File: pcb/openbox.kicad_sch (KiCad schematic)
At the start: 23 parts, among them J1 Conn_01x04_Male, J10 Conn_01x04_Male, J11 Conn_01x05_Male, J12 Conn_01x04_Male, J13 Conn_02x10_Odd_Even, J2 Conn_01x02_Male, J3 ST01x05, J4 ST01x05, J5 ST01x05, J6 ST01x05, J7 Conn_01x04_Male, J8 Conn_01x04_Male, J9 Conn_01x04_Male, U1 Pico, U2 SN74LV1T34DBV

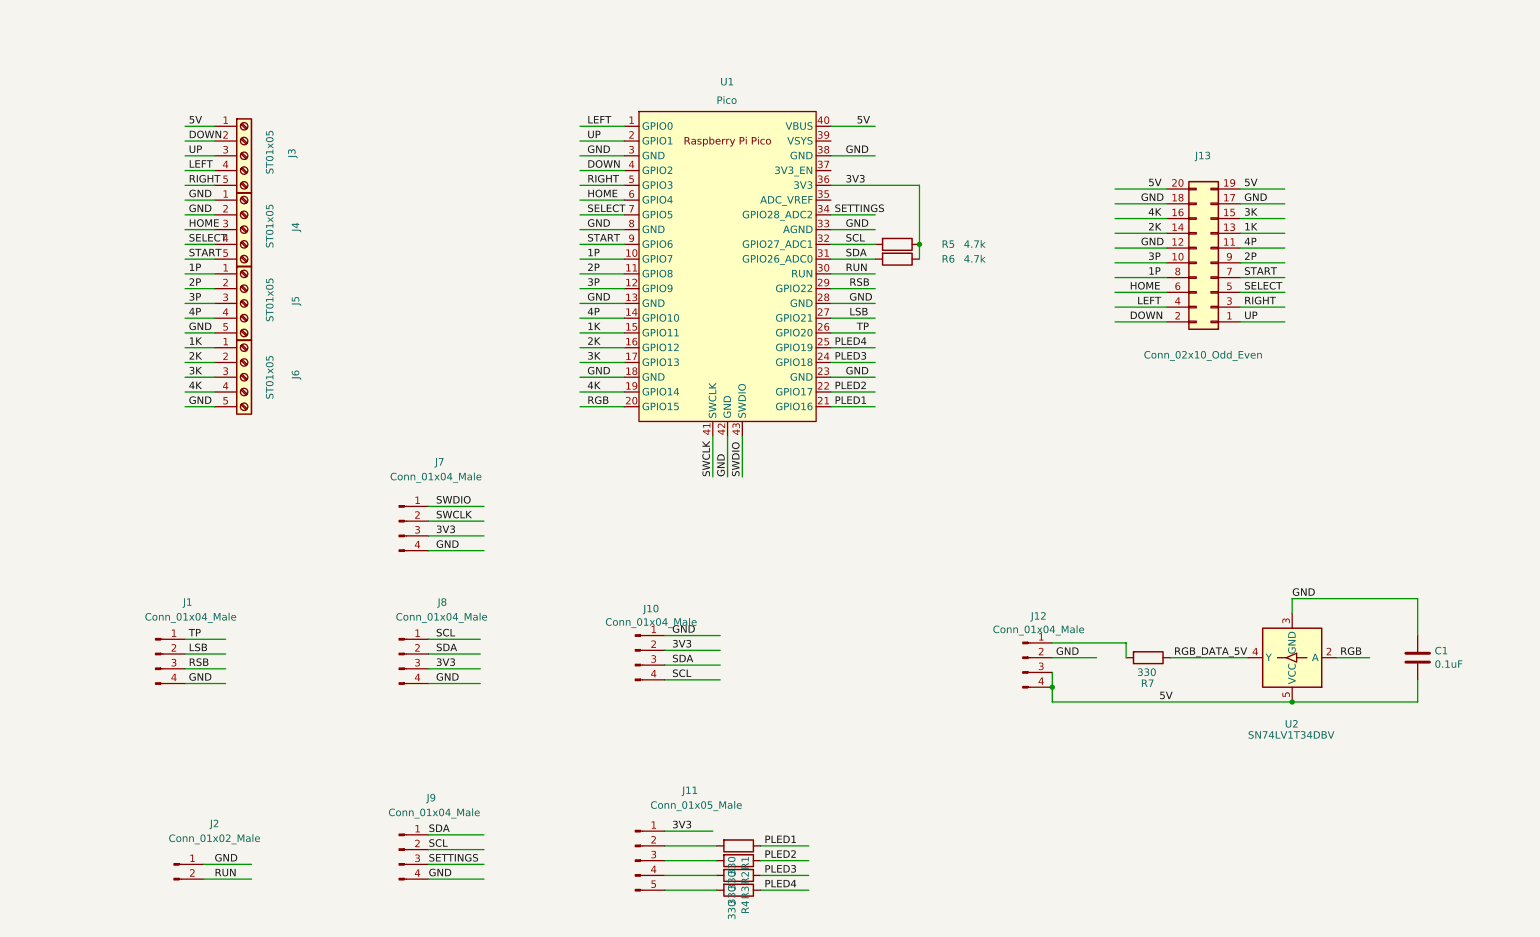
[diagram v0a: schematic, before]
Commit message: Pi placed, just have to place buttons
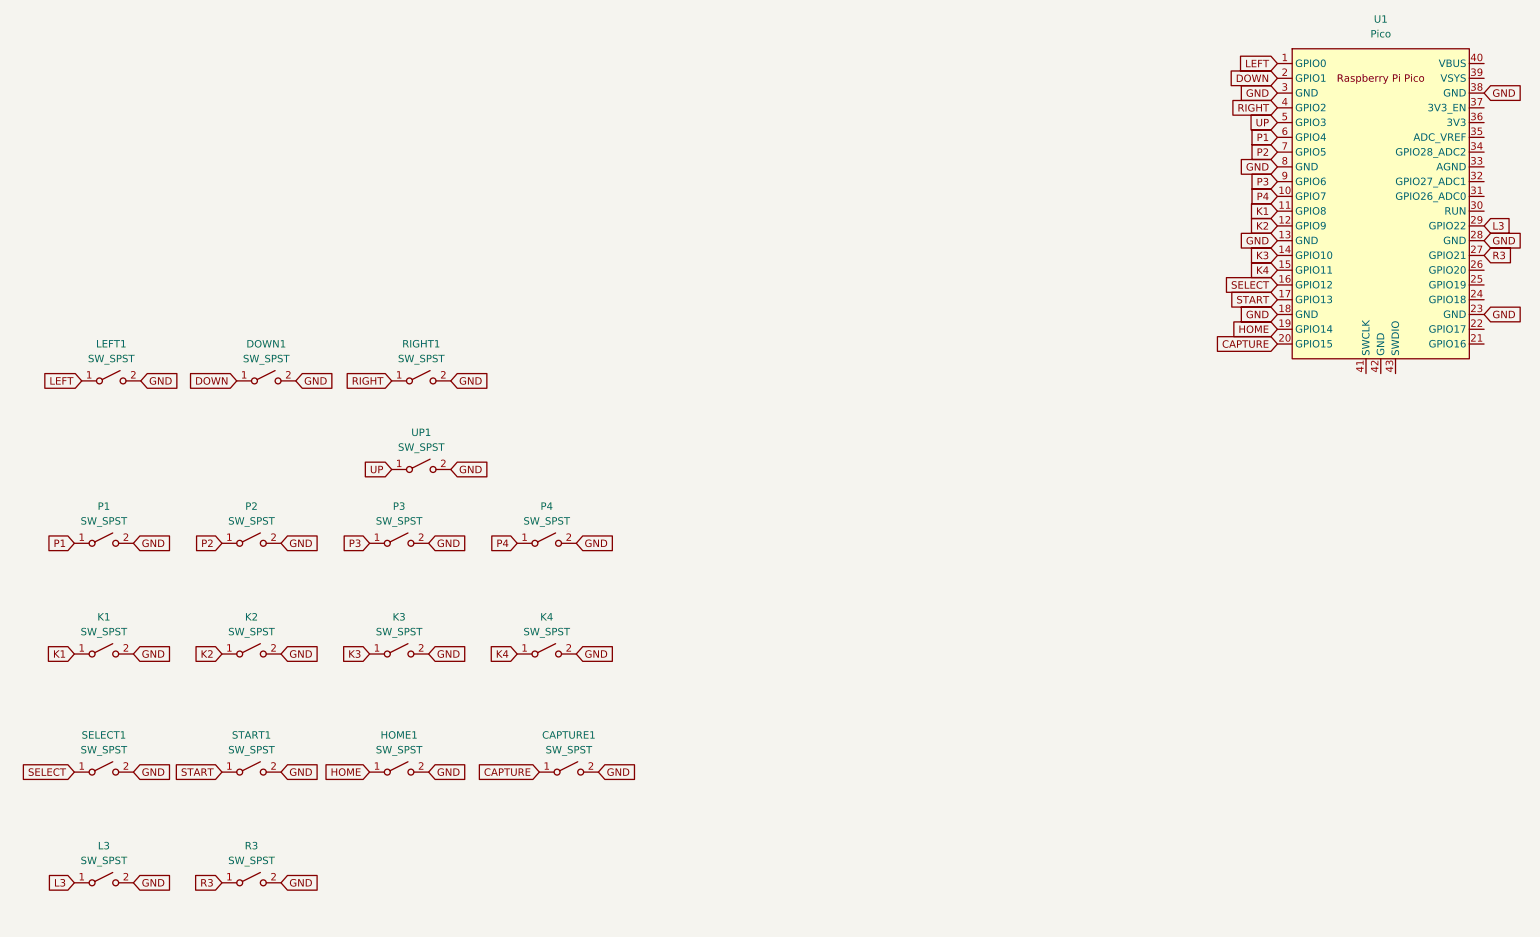
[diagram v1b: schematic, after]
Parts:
- removed C1: 0.1uF, Capacitor_SMD:C_0805_2012Metric, symbol Device:C
- removed J1, J10, J12, J9: Conn_01x04_Male, Connector_JST:JST_PH_B4B-PH-K_1x04_P2.00mm_Vertical, symbol Connector:Conn_01x04_Male
- removed J11: Conn_01x05_Male, Connector_JST:JST_PH_B5B-PH-K_1x05_P2.00mm_Vertical, symbol Connector:Conn_01x05_Male
- removed J13: Conn_02x10_Odd_Even, Connector_PinHeader_2.54mm:PinHeader_2x10_P2.54mm_Vertical, symbol Connector_Generic:Conn_02x10_Odd_Even
- removed J2: Conn_01x02_Male, Connector_PinHeader_2.54mm:PinHeader_1x02_P2.54mm_Vertical, symbol Connector:Conn_01x02_Male
- removed J3, J4, J5, J6: ST01x05, TerminalBlock_MetzConnect:TerminalBlock_MetzConnect_Type059_RT06305HBWC_1x05_P3.50mm_Horizontal, symbol Connector:Screw_Terminal_01x05
- removed J7, J8: Conn_01x04_Male, FeralAI:BOOM_SH_C145961_1x04_P1.00mm_Vertical, symbol Connector:Conn_01x04_Male
- removed R1, R2, R3, R4, R7: 330, Resistor_SMD:R_0805_2012Metric, symbol Device:R
- removed R5, R6: 4.7k, Resistor_SMD:R_0805_2012Metric, symbol Device:R
- removed U2: SN74LV1T34DBV, Package_TO_SOT_SMD:SOT-23-5, symbol Logic_LevelTranslator:SN74LV1T34DBV
- added CAPTURE1, DOWN1, HOME1, K1, K2, K3, K4, L3, LEFT1, P1, P2, P3, P4, R3, RIGHT1, SELECT1, START1, UP1: SW_SPST, keyswitches.pretty:Kailh_socket_PG1350, symbol Switch:SW_SPST
- U1: footprint MCU_RaspberryPi_and_Boards:RPi_Pico_SMD_TH_Clean -> MCU_RaspberryPi_and_Boards:RPi_Pico_SMD_TH
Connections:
- net 2K is gone; now on net SELECT: U1.16 (GPIO12)
- net 3K is gone; now on net START: U1.17 (GPIO13)
- net 4K is gone; now on net HOME: U1.19 (GPIO14)
- net DOWN: now also U1.2 (GPIO1), DOWN1.1 (A); no longer U1.4 (GPIO2)
- net GND: now also CAPTURE1.2 (B), DOWN1.2 (B), HOME1.2 (B), K1.2 (B), K2.2 (B), K3.2 (B), K4.2 (B), L3.2 (B), LEFT1.2 (B), P1.2 (B), P2.2 (B), P3.2 (B), P4.2 (B), R3.2 (B), RIGHT1.2 (B), SELECT1.2 (B), START1.2 (B), UP1.2 (B); no longer U1.33 (AGND), U1.42 (GND)
- net HOME: now also HOME1.1 (A); no longer U1.6 (GPIO4)
- net LEFT: now also LEFT1.1 (A)
- net RIGHT: now also U1.4 (GPIO2), RIGHT1.1 (A); no longer U1.5 (GPIO3)
- net SELECT: now also SELECT1.1 (A); no longer U1.7 (GPIO5)
- net START: now also START1.1 (A); no longer U1.9 (GPIO6)
- net UP: now also U1.5 (GPIO3), UP1.1 (A); no longer U1.2 (GPIO1)
- net 1K renamed K4
- net K4: now also K4.1 (A)
- net 1P renamed P4
- net P4: now also P4.1 (A)
- net 2P renamed K1
- net K1: now also K1.1 (A)
- net 3P renamed K2
- net K2: now also K2.1 (A)
- net 3V3: no longer names the net of U1.36 (3V3)
- net 4P renamed K3
- net K3: now also K3.1 (A)
- net 5V: no longer names the net of U1.40 (VBUS)
- net LSB renamed R3
- net R3: now also R3.1 (A)
- net PLED1: no longer names the net of U1.21 (GPIO16)
- net PLED2: no longer names the net of U1.22 (GPIO17)
- net PLED3: no longer names the net of U1.24 (GPIO18)
- net PLED4: no longer names the net of U1.25 (GPIO19)
- net RGB renamed CAPTURE
- net CAPTURE: now also CAPTURE1.1 (A)
- net RSB renamed L3
- net L3: now also L3.1 (A)
- net RUN: no longer names the net of U1.30 (RUN)
- net SCL: no longer names the net of U1.32 (GPIO27_ADC1)
- net SDA: no longer names the net of U1.31 (GPIO26_ADC0)
- net SETTINGS: no longer names the net of U1.34 (GPIO28_ADC2)
- net SWCLK: no longer names the net of U1.41 (SWCLK)
- net SWDIO: no longer names the net of U1.43 (SWDIO)
- net TP: no longer names the net of U1.26 (GPIO20)
- new net P1: P1.1 (A), U1.6 (GPIO4)
- new net P2: P2.1 (A), U1.7 (GPIO5)
- new net P3: P3.1 (A), U1.9 (GPIO6)

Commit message: Change extra buttons to 6x6mm push buttons
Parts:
- CAPTURE1, HOME1, L3, R3, SELECT1, START1: footprint keyswitches.pretty:Kailh_socket_PG1350 -> Button_Switch_THT:SW_PUSH_6mm
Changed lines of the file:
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@@
     (property "Reference" "START1" (id 0) (at 54.61 153.67 0))
     (property "Value" "SW_SPST" (id 1) (at 54.61 156.21 0))
-    (property "Footprint" "keyswitches.pretty:Kailh_socket_PG1350" (id 2) (at 54.61 160.02 0)
+    (property "Footprint" "Button_Switch_THT:SW_PUSH_6mm" (id 2) (at 54.61 160.02 0)
       (effects (font (size 1.27 1.27)) hide)
     )
@@
     (property "Reference" "HOME1" (id 0) (at 80.01 153.67 0))
     (property "Value" "SW_SPST" (id 1) (at 80.01 156.21 0))
-    (property "Footprint" "keyswitches.pretty:Kailh_socket_PG1350" (id 2) (at 80.01 160.02 0)
+    (property "Footprint" "Button_Switch_THT:SW_PUSH_6mm" (id 2) (at 80.01 160.02 0)
       (effects (font (size 1.27 1.27)) hide)
     )
@@
     (property "Reference" "CAPTURE1" (id 0) (at 109.22 153.67 0))
     (property "Value" "SW_SPST" (id 1) (at 109.22 156.21 0))
-    (property "Footprint" "keyswitches.pretty:Kailh_socket_PG1350" (id 2) (at 109.22 160.02 0)
+    (property "Footprint" "Button_Switch_THT:SW_PUSH_6mm" (id 2) (at 109.22 160.02 0)
       (effects (font (size 1.27 1.27)) hide)
     )
@@
     (property "Reference" "SELECT1" (id 0) (at 29.21 153.67 0))
     (property "Value" "SW_SPST" (id 1) (at 29.21 156.21 0))
-    (property "Footprint" "keyswitches.pretty:Kailh_socket_PG1350" (id 2) (at 29.21 160.02 0)
+    (property "Footprint" "Button_Switch_THT:SW_PUSH_6mm" (id 2) (at 29.21 160.02 0)
       (effects (font (size 1.27 1.27)) hide)
     )
@@
     (property "Reference" "L3" (id 0) (at 29.21 172.72 0))
     (property "Value" "SW_SPST" (id 1) (at 29.21 175.26 0))
-    (property "Footprint" "keyswitches.pretty:Kailh_socket_PG1350" (id 2) (at 29.21 179.07 0)
+    (property "Footprint" "Button_Switch_THT:SW_PUSH_6mm" (id 2) (at 29.21 179.07 0)
       (effects (font (size 1.27 1.27)) hide)
     )
@@
     (property "Reference" "R3" (id 0) (at 54.61 172.72 0))
     (property "Value" "SW_SPST" (id 1) (at 54.61 175.26 0))
-    (property "Footprint" "keyswitches.pretty:Kailh_socket_PG1350" (id 2) (at 54.61 179.07 0)
+    (property "Footprint" "Button_Switch_THT:SW_PUSH_6mm" (id 2) (at 54.61 179.07 0)
       (effects (font (size 1.27 1.27)) hide)
     )
@@
   (symbol_instances
     (path "/542d0816-e5c3-4b0c-9fe6-a8befec1abb6"
-      (reference "CAPTURE1") (unit 1) (value "SW_SPST") (footprint "keyswitches.pretty:Kailh_socket_PG1350")
+      (reference "CAPTURE1") (unit 1) (value "SW_SPST") (footprint "Button_Switch_THT:SW_PUSH_6mm")
     )
     (path "/95df881d-f66e-40ba-bb34-b870660a1b3b"
@@
     )
     (path "/3f368872-dbe5-48d5-b1bb-c08d1f5e0dd2"
-      (reference "HOME1") (unit 1) (value "SW_SPST") (footprint "keyswitches.pretty:Kailh_socket_PG1350")
+      (reference "HOME1") (unit 1) (value "SW_SPST") (footprint "Button_Switch_THT:SW_PUSH_6mm")
     )
     (path "/736c80fe-01fb-4783-a2be-9e16fccbf781"
@@
     )
     (path "/f1b2b416-be79-4848-8079-c1cc5017a182"
-      (reference "L3") (unit 1) (value "SW_SPST") (footprint "keyswitches.pretty:Kailh_socket_PG1350")
+      (reference "L3") (unit 1) (value "SW_SPST") (footprint "Button_Switch_THT:SW_PUSH_6mm")
     )
     (path "/8c2504d2-1b97-4d06-946f-3cb4a9d80e8a"
@@
     )
     (path "/f8df1ab9-c821-41ea-baed-1980e5d9f217"
-      (reference "R3") (unit 1) (value "SW_SPST") (footprint "keyswitches.pretty:Kailh_socket_PG1350")
+      (reference "R3") (unit 1) (value "SW_SPST") (footprint "Button_Switch_THT:SW_PUSH_6mm")
     )
     (path "/6087dd73-6174-4d62-9d84-8dd5c28de338"
@@
     )
     (path "/c40dde26-fffd-4a43-a9b1-f178e1e494f3"
-      (reference "SELECT1") (unit 1) (value "SW_SPST") (footprint "keyswitches.pretty:Kailh_socket_PG1350")
+      (reference "SELECT1") (unit 1) (value "SW_SPST") (footprint "Button_Switch_THT:SW_PUSH_6mm")
     )
     (path "/3c4412bc-b78d-459f-9f44-573a3673fb1a"
-      (reference "START1") (unit 1) (value "SW_SPST") (footprint "keyswitches.pretty:Kailh_socket_PG1350")
+      (reference "START1") (unit 1) (value "SW_SPST") (footprint "Button_Switch_THT:SW_PUSH_6mm")
     )
     (path "/b7eb2cfe-700a-4d22-b46a-0c15d5da00dc"
